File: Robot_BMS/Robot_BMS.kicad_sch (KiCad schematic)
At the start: 0 parts

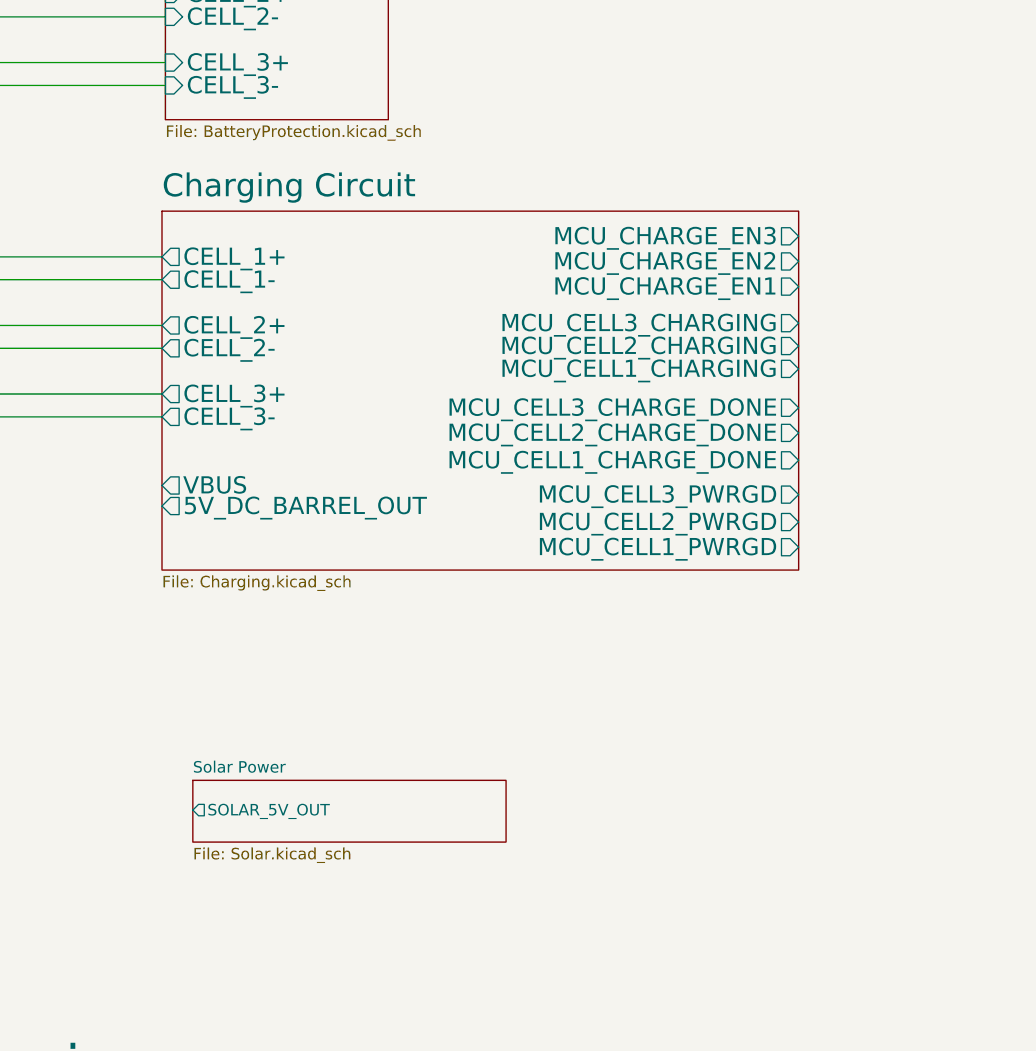
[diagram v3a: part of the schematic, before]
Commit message: solar charger set to 15V
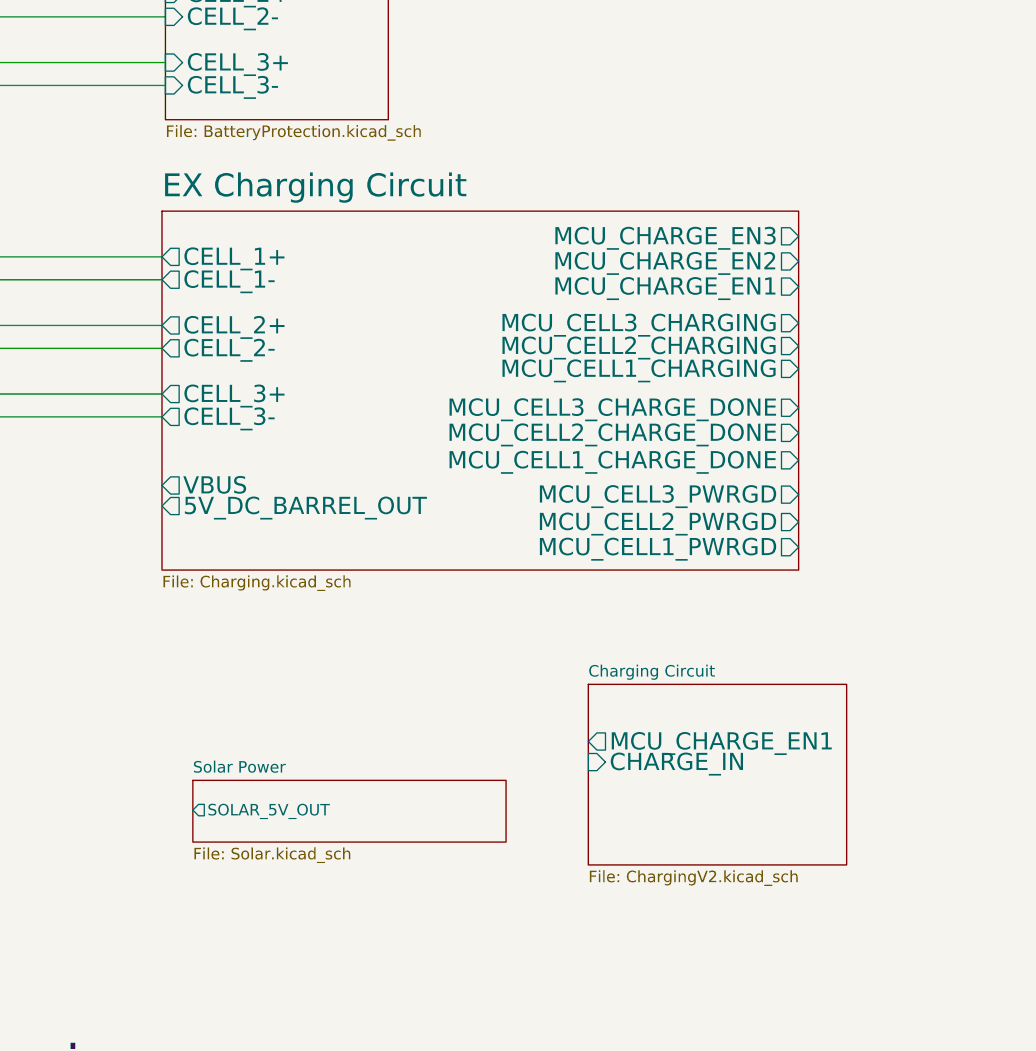
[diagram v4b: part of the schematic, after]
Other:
- added sheet EX Charging Circuit (Charging.kicad_sch)
- sheet Charging Circuit: file Charging.kicad_sch -> ChargingV2.kicad_sch
- sheet Charging Circuit ports: added CHARGE_IN; removed 5V_DC_BARREL_OUT, CELL_1+, CELL_1-, CELL_2+, CELL_2-, CELL_3+, CELL_3-, MCU_CELL1_CHARGE_DONE, MCU_CELL1_CHARGING, MCU_CELL1_PWRGD, MCU_CELL2_CHARGE_DONE, MCU_CELL2_CHARGING, MCU_CELL2_PWRGD, MCU_CELL3_CHARGE_DONE, MCU_CELL3_CHARGING, MCU_CELL3_PWRGD, MCU_CHARGE_EN2, MCU_CHARGE_EN3, VBUS
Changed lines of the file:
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@@
+	)
+	(sheet
+		(at 176.53 135.128)
+		(size 28.702 20.066)
+		(fields_autoplaced yes)
+		(stroke
+			(width 0.1524)
+			(type solid)
+		)
+		(fill
+			(color 255 171 167 1.0000)
+		)
+		(property "Sheetname" "Charging Circuit"
+			(at 176.53 134.4164 0)
+			(effects
+				(font
+					(size 1.27 1.27)
+				)
+				(justify left bottom)
+			)
+		)
+		(property "Sheetfile" "ChargingV2.kicad_sch"
+			(at 176.53 155.7786 0)
+			(effects
+				(font
+					(size 1.27 1.27)
+				)
+				(justify left top)
+			)
+		)
+		(pin "MCU_CHARGE_EN1" output
+			(at 176.53 141.478 180)
+			(effects
+				(font
+					(size 1.905 1.905)
+				)
+				(justify left)
+			)
+		)
+		(pin "CHARGE_IN" input
+			(at 176.53 143.764 180)
+			(effects
+				(font
+					(size 1.905 1.905)
+				)
+				(justify left)
+			)
+		)
+		(instances
+			(project "Robot_BMS"
+				(path "/72551b1c-3d40-4199-8911-e5b015f4abec"
+					(page "4")
+				)
+			)
+		)
 	)
 	(sheet
@@
 			(color 76 253 255 1.0000)
 		)
-		(property "Sheetname" "Charging Circuit"
+		(property "Sheetname" "EX Charging Circuit"
 			(at 129.159 81.2034 0)
 			(effects
@@
 			(project "Robot_BMS"
 				(path "/72551b1c-3d40-4199-8911-e5b015f4abec"
-					(page "4")
-				)
-			)
+					(page "11")
+				)
+			)

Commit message: ex charging circuit last appearence
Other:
- sheet DC Power Supply renamed DC Barrel Jack
- sheet DC Barrel Jack ports: added DC_BARREL_JACK; removed 5V_DC_BARREL_OUT
- sheet Solar Power ports: added SOLAR_13V_OUT; removed SOLAR_5V_OUT
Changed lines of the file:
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@@
 	)
 	(sheet
-		(at 229.87 69.088)
-		(size 29.718 18.796)
+		(at 229.87 75.184)
+		(size 29.718 4.826)
 		(fields_autoplaced yes)
 		(stroke
@@
 			(color 255 32 234 1.0000)
 		)
-		(property "Sheetname" "DC Power Supply"
-			(at 229.87 68.3764 0)
+		(property "Sheetname" "DC Barrel Jack"
+			(at 229.87 74.4724 0)
 			(effects
 				(font
@@
 		)
 		(property "Sheetfile" "DC_Barrel_Jack.kicad_sch"
-			(at 229.87 88.4686 0)
+			(at 229.87 80.5946 0)
 			(effects
 				(font
@@
 			)
 		)
-		(pin "5V_DC_BARREL_OUT" output
-			(at 229.87 75.184 180)
-			(effects
-				(font
-					(size 1.905 1.905)
+		(pin "DC_BARREL_JACK" output
+			(at 229.87 77.724 180)
+			(effects
+				(font
+					(size 1.27 1.27)
 				)
 				(justify left)
@@
 			)
 		)
-		(pin "SOLAR_5V_OUT" output
-			(at 132.588 149.098 180)
-			(effects
-				(font
+		(pin "SOLAR_13V_OUT" output
+			(at 132.588 149.606 180)
+			(effects
+				(font

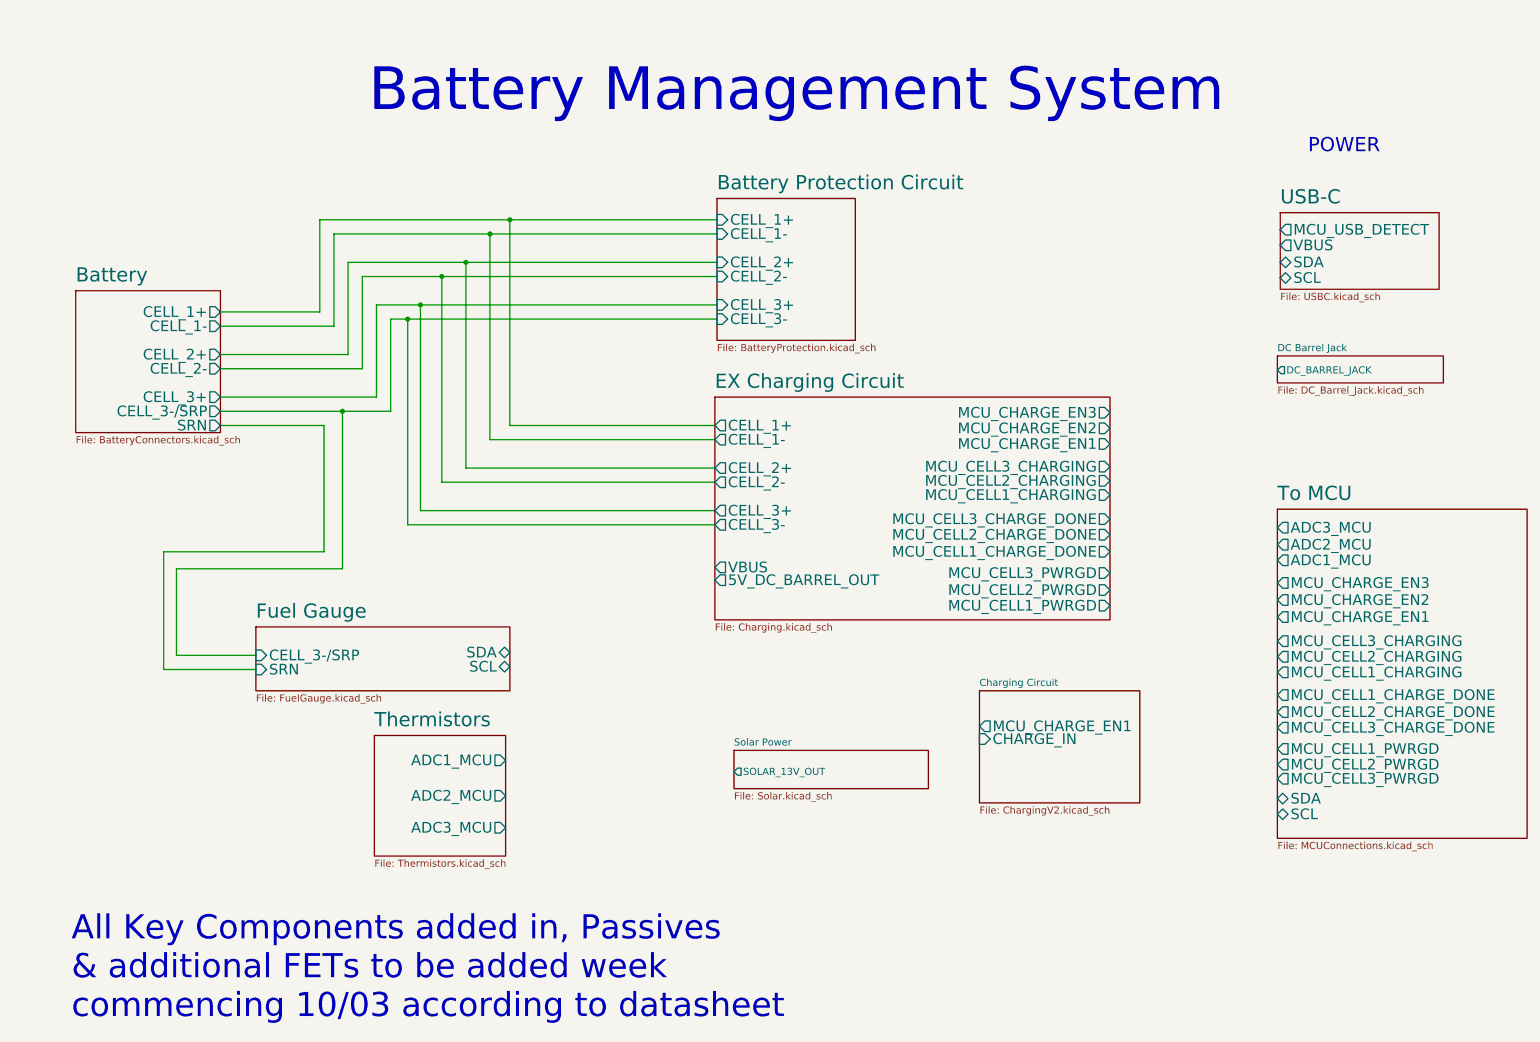
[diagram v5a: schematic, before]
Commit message: battery management ic is being added
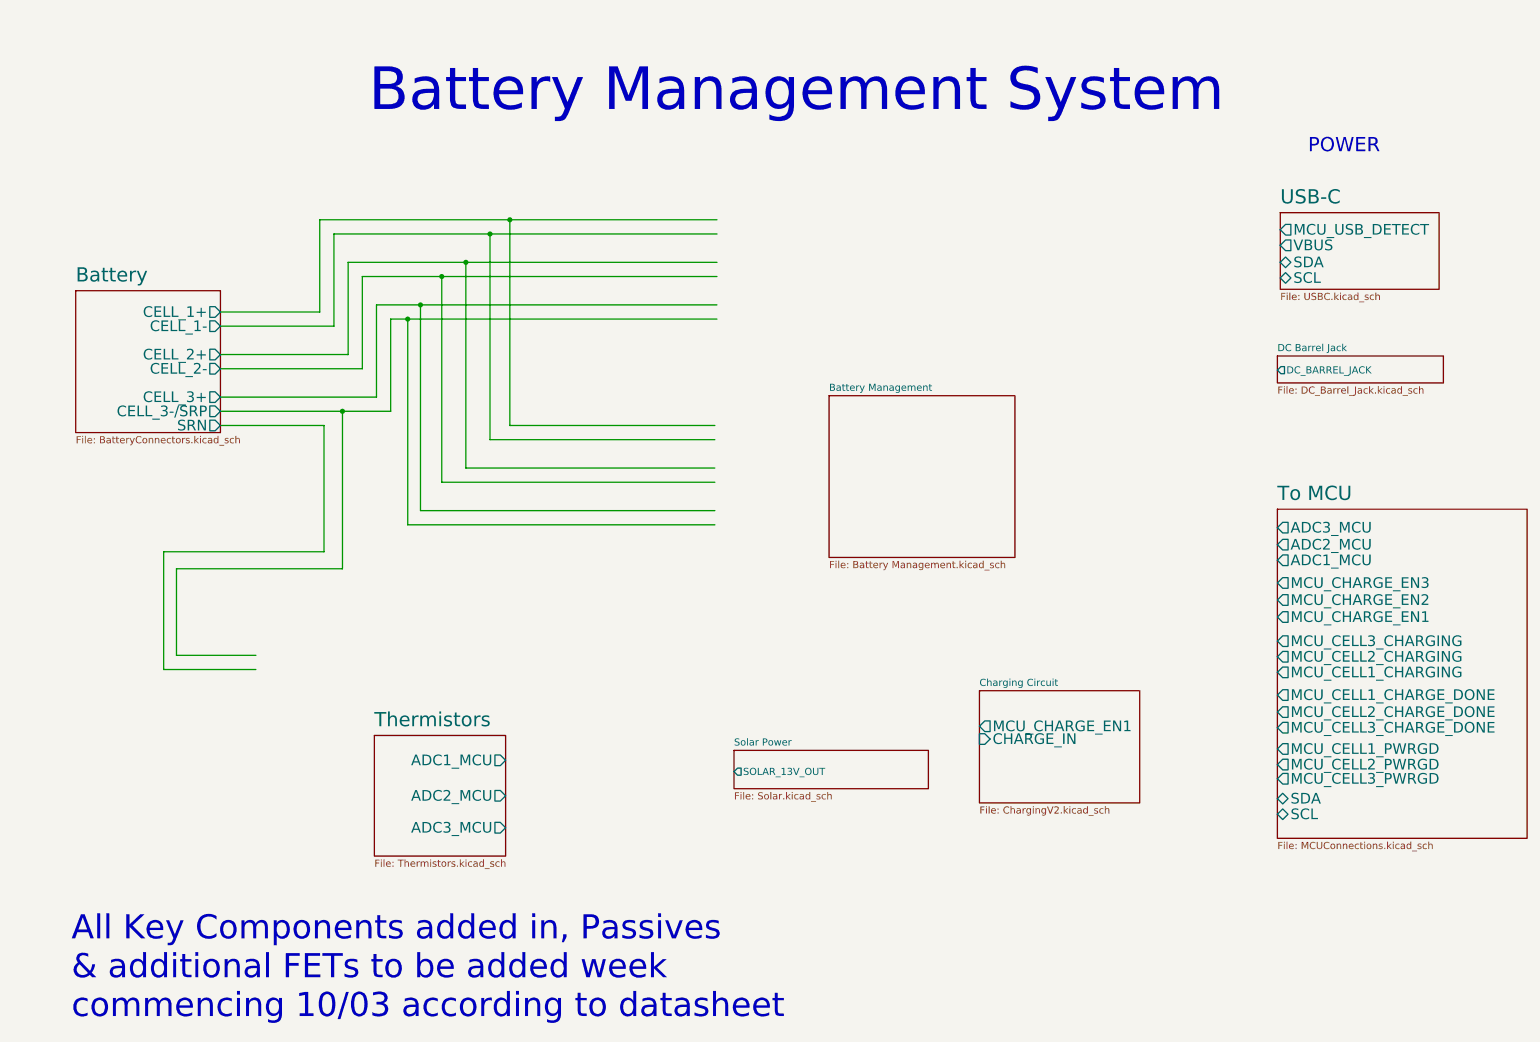
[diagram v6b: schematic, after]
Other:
- removed sheet Battery Protection Circuit
- removed sheet EX Charging Circuit
- removed sheet Fuel Gauge
- added sheet Battery Management (Battery Management.kicad_sch)

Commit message: System drawing down on top schematic, will start inputting footprints
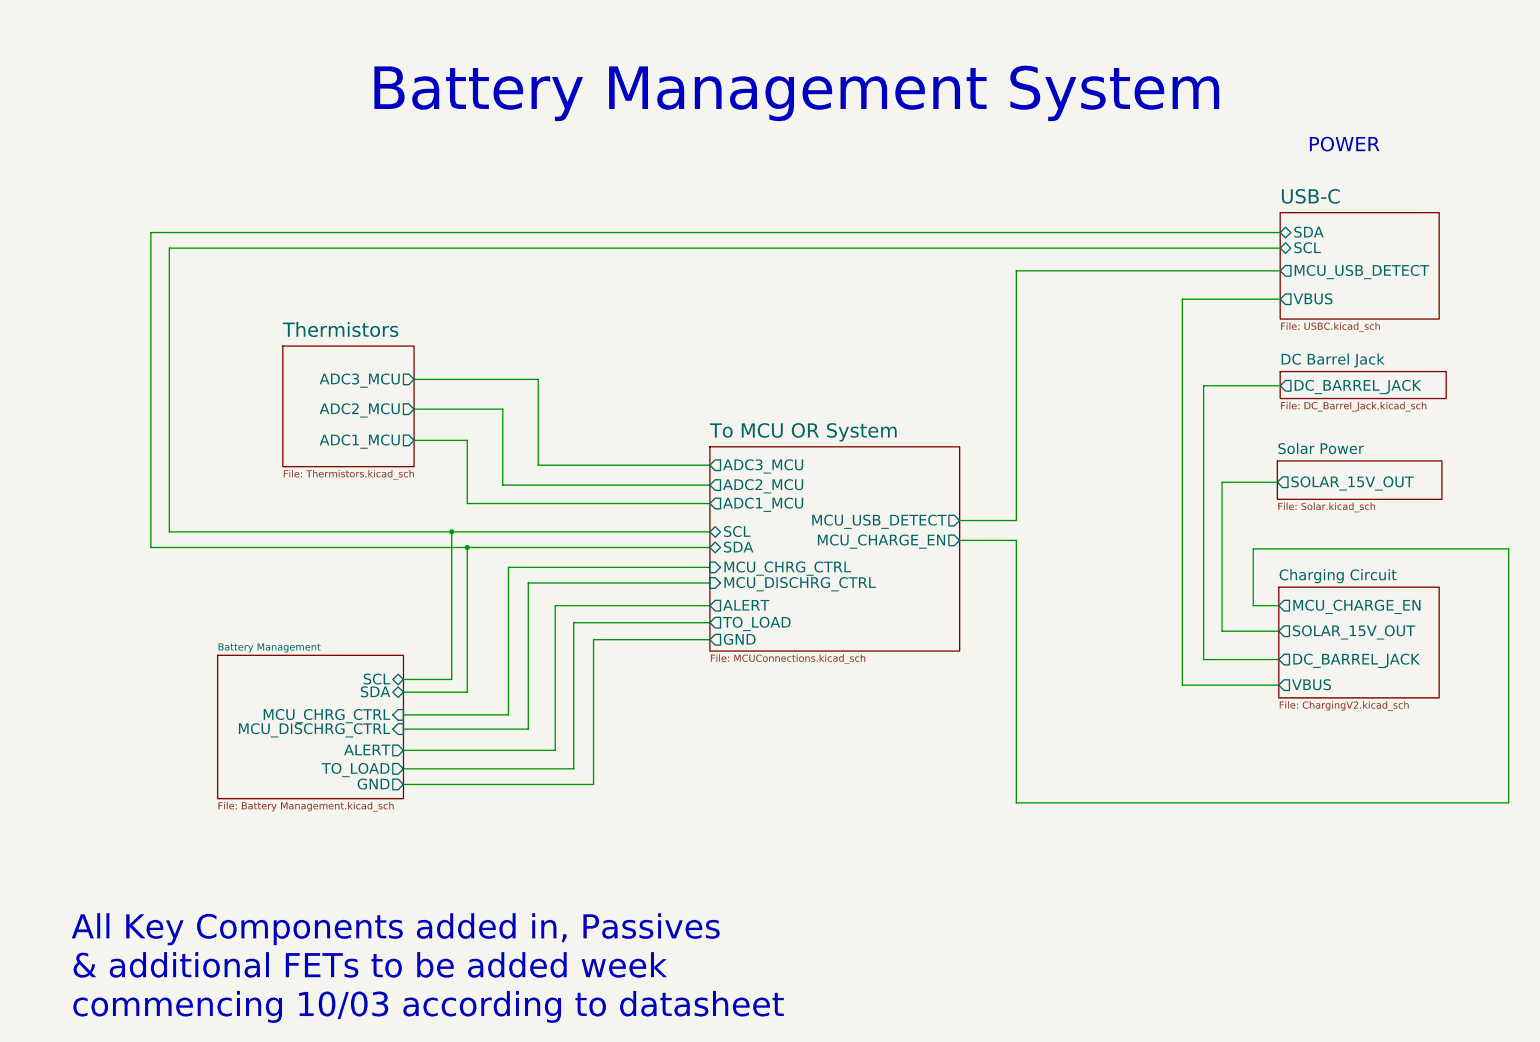
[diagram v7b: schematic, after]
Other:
- sheet To MCU renamed To MCU OR System
- removed sheet Battery
- sheet Battery Management ports: added ALERT, GND, MCU_CHRG_CTRL, MCU_DISCHRG_CTRL, SCL, SDA, TO_LOAD; removed none
- sheet Charging Circuit ports: added DC_BARREL_JACK, MCU_CHARGE_EN, SOLAR_15V_OUT, VBUS; removed CHARGE_IN, MCU_CHARGE_EN1
- sheet Solar Power ports: added SOLAR_15V_OUT; removed SOLAR_13V_OUT
- sheet To MCU OR System ports: added ALERT, GND, MCU_CHARGE_EN, MCU_CHRG_CTRL, MCU_DISCHRG_CTRL, MCU_USB_DETECT, TO_LOAD; removed MCU_CELL1_CHARGE_DONE, MCU_CELL1_CHARGING, MCU_CELL1_PWRGD, MCU_CELL2_CHARGE_DONE, MCU_CELL2_CHARGING, MCU_CELL2_PWRGD, MCU_CELL3_CHARGE_DONE, MCU_CELL3_CHARGING, MCU_CELL3_PWRGD, MCU_CHARGE_EN1, MCU_CHARGE_EN2, MCU_CHARGE_EN3

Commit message: adding footprints and actual passive components
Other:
- sheet Thermistors ports: added 3V3; removed none
- sheet To MCU OR System ports: added 3V3; removed none
- note removed: "All Key Components added in, Passives & additional FETs to be added week commencing 10/03 according to datasheet"
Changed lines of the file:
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@@
 	(wire
 		(pts
-			(xy 84.836 90.297) (xy 75.311 90.297)
+			(xy 84.836 90.297) (xy 74.676 90.297)
 		)
 		(stroke
@@
 	(wire
 		(pts
+			(xy 74.676 74.422) (xy 107.188 74.422)
+		)
+		(stroke
+			(width 0)
+			(type default)
+		)
+	)
+	(wire
+		(pts
 			(xy 225.552 119.888) (xy 225.552 109.728)
 		)
@@
 	(wire
 		(pts
-			(xy 97.536 79.375) (xy 75.311 79.375)
+			(xy 107.188 74.422) (xy 107.188 90.678)
+		)
+		(stroke
+			(width 0)
+			(type default)
+		)
+	)
+	(wire
+		(pts
+			(xy 97.536 79.375) (xy 74.676 79.375)
 		)
 		(stroke
@@
 	(wire
 		(pts
+			(xy 107.188 90.678) (xy 128.27 90.678)
+		)
+		(stroke
+			(width 0)
+			(type default)
+		)
+	)
+	(wire
+		(pts
 			(xy 91.186 84.709) (xy 91.186 98.298)
 		)
@@
 	(wire
 		(pts
-			(xy 75.311 84.709) (xy 91.186 84.709)
+			(xy 74.676 84.709) (xy 91.186 84.709)
 		)
 		(stroke
@@
 	(text "Battery Management System"
 		(exclude_from_sim no)
-		(at 143.764 27.686 0)
+		(at 98.806 21.59 0)
 		(effects
 			(font
 				(size 7.62 7.62)
 			)
-		)
-	)
-	(text "All Key Components added in, Passives \n& additional FETs to be added week \ncommencing 10/03 according to datasheet"
-		(exclude_from_sim no)
-		(at 13.97 184.658 0)
-		(effects
-			(font
-				(size 4.318 4.318)
-			)
-			(justify left)
 		)
 	)
@@
 	)
 	(sheet
-		(at 51.816 73.406)
-		(size 23.495 21.59)
+		(at 51.181 72.39)
+		(size 23.495 22.606)
 		(fields_autoplaced yes)
 		(stroke
@@
 		)
 		(property "Sheetname" "Thermistors"
-			(at 51.816 72.0594 0)
+			(at 51.181 71.0434 0)
 			(effects
 				(font
@@
 		)
 		(property "Sheetfile" "Thermistors.kicad_sch"
-			(at 51.816 95.5806 0)
+			(at 51.181 95.5806 0)
 			(effects
 				(font
@@
 		)
 		(pin "ADC2_MCU" output
-			(at 75.311 84.709 0)
+			(at 74.676 84.709 0)
 			(effects
 				(font
@@
 		)
 		(pin "ADC3_MCU" output
-			(at 75.311 79.375 0)
+			(at 74.676 79.375 0)
 			(effects
 				(font
@@
 		)
 		(pin "ADC1_MCU" output
-			(at 75.311 90.297 0)
+			(at 74.676 90.297 0)
+			(effects
+				(font
+					(size 1.905 1.905)
+				)
+				(justify right)
+			)
+		)
+		(pin "3V3" input
+			(at 74.676 74.422 0)
 			(effects
 				(font
@@
 	)
 	(sheet
-		(at 128.27 91.44)
-		(size 44.704 36.576)
+		(at 128.27 87.884)
+		(size 44.704 40.132)
 		(fields_autoplaced yes)
 		(stroke
@@
 		)
 		(property "Sheetname" "To MCU OR System"
-			(at 128.27 90.0934 0)
+			(at 128.27 86.5374 0)
 			(effects
 				(font
@@
 			(effects
 				(font
+					(size 1.905 1.905)
+				)
+				(justify left)
+			)
+		)
+		(pin "3V3" input
+			(at 128.27 90.678 180)
+			(effects
+				(font
